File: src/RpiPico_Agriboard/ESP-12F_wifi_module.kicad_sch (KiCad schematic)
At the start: 12 parts, among them J27 Conn_02x05_Odd_Even, SW3 SW_Push, SW4 SW_Push, U4 ESP-12F

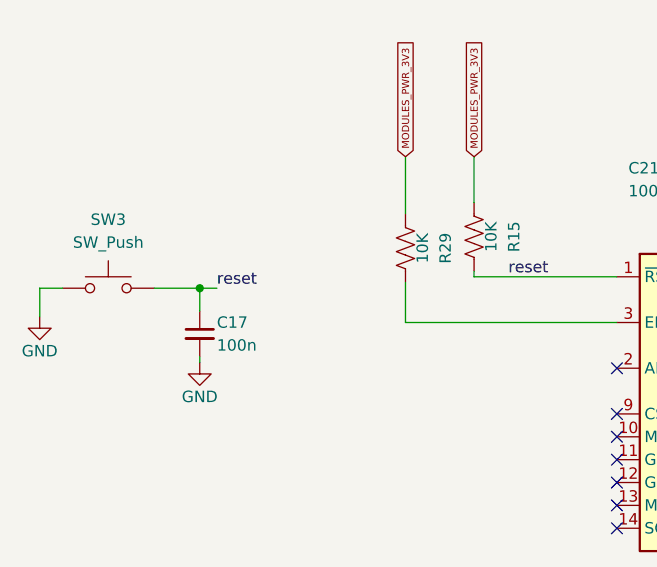
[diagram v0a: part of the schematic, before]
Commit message: power module supply line increase and reupdates on schematic
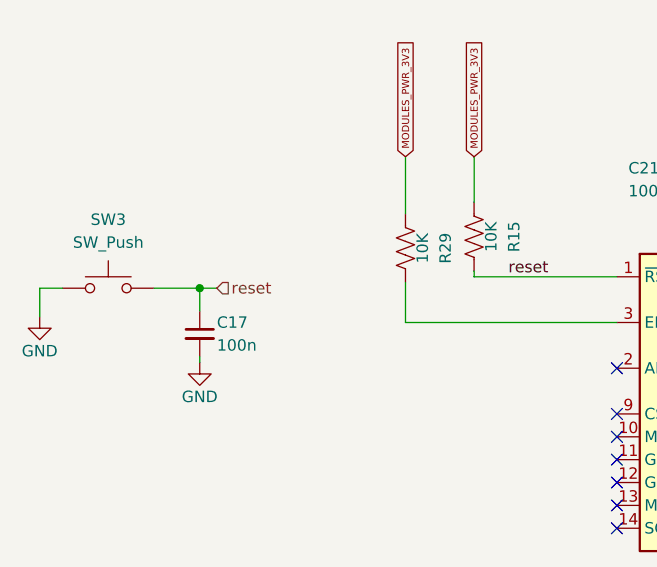
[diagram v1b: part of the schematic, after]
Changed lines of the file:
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@@
   (no_connect (at 154.94 78.74))
   (no_connect (at 154.94 91.44))
+  (wire (pts (xy 108.585 66.04) (xy 124.46 66.04))
+    (stroke (width 0) (type default))
+  )
   (wire (pts (xy 212.09 106.045) (xy 217.17 106.045))
     (stroke (width 0) (type default))
@@
   )
   (wire (pts (xy 186.69 103.505) (xy 199.39 103.505))
-    (stroke (width 0) (type default))
-  )
-  (wire (pts (xy 108.585 66.04) (xy 124.46 66.04))
     (stroke (width 0) (type default))
   )
@@
     (effects (font (size 1.27 1.27)) (justify left bottom))
   )
-  (label "reset" (at 80.01 67.31 0) (fields_autoplaced)
-    (effects (font (size 1.27 1.27)) (justify left bottom))
-  )
   (label "TDI" (at 164.465 81.28 0) (fields_autoplaced)
     (effects (font (size 1.27 1.27)) (justify left bottom))
@@
     (effects (font (size 1.27 1.27) bold) (justify left))
   )
+  (hierarchical_label "reset" (shape input) (at 80.01 67.31 0) (fields_autoplaced)
+    (effects (font (size 1.27 1.27)) (justify left))
+  )
   (hierarchical_label "ESP8266_TX_out" (shape input) (at 217.17 100.965 0) (fields_autoplaced)
